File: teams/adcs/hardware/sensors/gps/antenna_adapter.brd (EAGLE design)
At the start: 17.8 x 12.4 mm, 2 parts

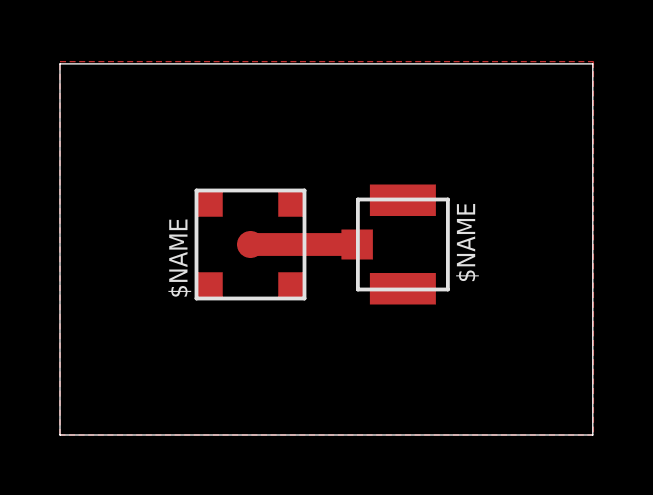
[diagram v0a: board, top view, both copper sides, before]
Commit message: ADCS/GPS: Revise GPS antenna coupler with new footprints
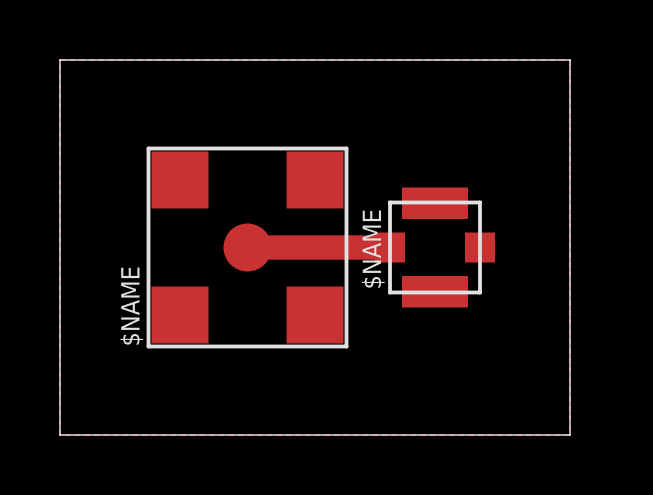
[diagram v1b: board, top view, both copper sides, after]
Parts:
- U$1: value CONN_MMCX -> CONN_MCX; device DubSat1 Components:MMCX_JACK_FEMALE_SMD -> DubSat1 Components:MCX_JACK_FEMALE_SMD
- U$2: value CONN_U.FL -> CONN_UMC; device DubSat1 Components:U.FL_JACK_MALE_SMD -> DubSat1 Components:UMC_JACK_MALE_SMD
- moved U$2 1.07 mm to (12.5, 6.25), turned to 270 degrees
- moved U$1 0.14 mm to (6.25, 6.25)
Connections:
- net GND: now also U$1.GND@1, U$1.GND@2, U$1.GND@3, U$1.GND@4, U$2.GND@1, U$2.GND@2, U$2.GND@3; no longer U$1.P$2, U$1.P$3, U$1.P$4, U$1.P$5, U$2.P$2, U$2.P$3
- net SIG: now also U$1.SIG, U$2.SIG; no longer U$1.P$1, U$2.P$1
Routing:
- net SIG: track 3.55 -> 4.75 mm
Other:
- board size 17.8 x 12.4 mm -> 17 x 12.5 mm
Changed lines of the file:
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@@
 <?xml version="1.0" encoding="utf-8"?>
 <!DOCTYPE eagle SYSTEM "eagle.dtd">
-<eagle version="8.6.0">
+<eagle version="8.6.2">
 <drawing>
 <settings>
@@
 <setting verticaltext="up"/>
 </settings>
-<grid distance="50" unitdist="mil" unit="mil" style="lines" multiple="1" display="no" altdistance="5" altunitdist="mil" altunit="mil"/>
+<grid distance="1" unitdist="mm" unit="mm" style="lines" multiple="1" display="no" altdistance="0.25" altunitdist="mm" altunit="mm"/>
 <layers>
 <layer number="1" name="Top" color="4" fill="1" visible="yes" active="yes"/>
@@
 <board>
 <plain>
-<wire x1="0" y1="0" x2="17.76" y2="0" width="0" layer="20"/>
-<wire x1="17.76" y1="0" x2="17.76" y2="12.37" width="0" layer="20"/>
-<wire x1="17.76" y1="12.37" x2="0" y2="12.37" width="0" layer="20"/>
-<wire x1="0" y1="12.37" x2="0" y2="0" width="0" layer="20"/>
+<wire x1="0" y1="0" x2="17" y2="0" width="0" layer="20"/>
+<wire x1="17" y1="0" x2="17" y2="12.5" width="0" layer="20"/>
+<wire x1="17" y1="12.5" x2="0" y2="12.5" width="0" layer="20"/>
+<wire x1="0" y1="12.5" x2="0" y2="0" width="0" layer="20"/>
 </plain>
 <attributes>
@@
 <param name="mtCopper" value="0.035mm 0.035mm 0.035mm 0.035mm 0.035mm 0.035mm 0.035mm 0.035mm 0.035mm 0.035mm 0.035mm 0.035mm 0.035mm 0.035mm 0.035mm 0.035mm"/>
 <param name="mtIsolate" value="1.5mm 0.15mm 0.2mm 0.15mm 0.2mm 0.15mm 0.2mm 0.15mm 0.2mm 0.15mm 0.2mm 0.15mm 0.2mm 0.15mm 0.2mm"/>
-<param name="mdWireWire" value="14mil"/>
-<param name="mdWirePad" value="14mil"/>
-<param name="mdWireVia" value="14mil"/>
-<param name="mdPadPad" value="14mil"/>
-<param name="mdPadVia" value="14mil"/>
-<param name="mdViaVia" value="14mil"/>
+<param name="mdWireWire" value="30mil"/>
+<param name="mdWirePad" value="30mil"/>
+<param name="mdWireVia" value="30mil"/>
+<param name="mdPadPad" value="30mil"/>
+<param name="mdPadVia" value="30mil"/>
+<param name="mdViaVia" value="30mil"/>
 <param name="mdSmdPad" value="14mil"/>
 <param name="mdSmdVia" value="14mil"/>
@@
 </autorouter>
 <elements>
-<element name="U$1" library="DubSat1 Components" package="MMCX_JACK_FEMALE_SMD" value="CONN_MMCX" x="6.35" y="6.35"/>
-<element name="U$2" library="DubSat1 Components" package="U.FL_JACK_MALE_SMD" value="CONN_U.FL" x="11.43" y="6.35" rot="R180"/>
+<element name="U$1" library="DubSat1 Components" package="MCX_JACK_FEMALE_SMD" value="CONN_MCX" x="6.25" y="6.25"/>
+<element name="U$2" library="DubSat1 Components" package="UMC_JACK_MALE_SMD" value="CONN_UMC" x="12.5" y="6.25" rot="R270"/>
 </elements>
 <signals>
 <signal name="SIG">
-<contactref element="U$2" pad="P$1"/>
-<contactref element="U$1" pad="P$1"/>
-<wire x1="6.35" y1="6.35" x2="9.905" y2="6.35" width="0.762" layer="1"/>
+<contactref element="U$2" pad="SIG"/>
+<contactref element="U$1" pad="SIG"/>
+<wire x1="6.25" y1="6.25" x2="11" y2="6.25" width="0.8128" layer="1"/>
 </signal>
 <signal name="GND">
-<contactref element="U$2" pad="P$2"/>
-<contactref element="U$2" pad="P$3"/>
-<contactref element="U$1" pad="P$2"/>
-<contactref element="U$1" pad="P$3"/>
-<contactref element="U$1" pad="P$4"/>
-<contactref element="U$1" pad="P$5"/>
-<polygon width="0.254" layer="1">
-<vertex x="0" y="12.446"/>
-<vertex x="17.78" y="12.446"/>
-<vertex x="17.78" y="0"/>
+<contactref element="U$2" pad="GND@1"/>
+<contactref element="U$2" pad="GND@2"/>
+<contactref element="U$1" pad="GND@1"/>
+<contactref element="U$1" pad="GND@2"/>
+<contactref element="U$1" pad="GND@3"/>
+<contactref element="U$1" pad="GND@4"/>
+<polygon width="0.254" layer="1" thermals="no">
+<vertex x="0" y="12.5"/>
+<vertex x="17" y="12.5"/>
+<vertex x="17" y="0"/>
 <vertex x="0" y="0"/>
 </polygon>
+<contactref element="U$2" pad="GND@3"/>
 </signal>
 </signals>
